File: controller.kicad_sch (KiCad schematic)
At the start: 57 parts, among them J1 Conn_ST_STDC14, J2 USB_C_Receptacle_USB2.0_14P, SW1 SW_Push, SW10 SW_Push, SW11 SW_Push, SW12 SW_Push, SW13 SW_Push, SW2 SW_Push, SW3 SW_Push, SW4 SW_Push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

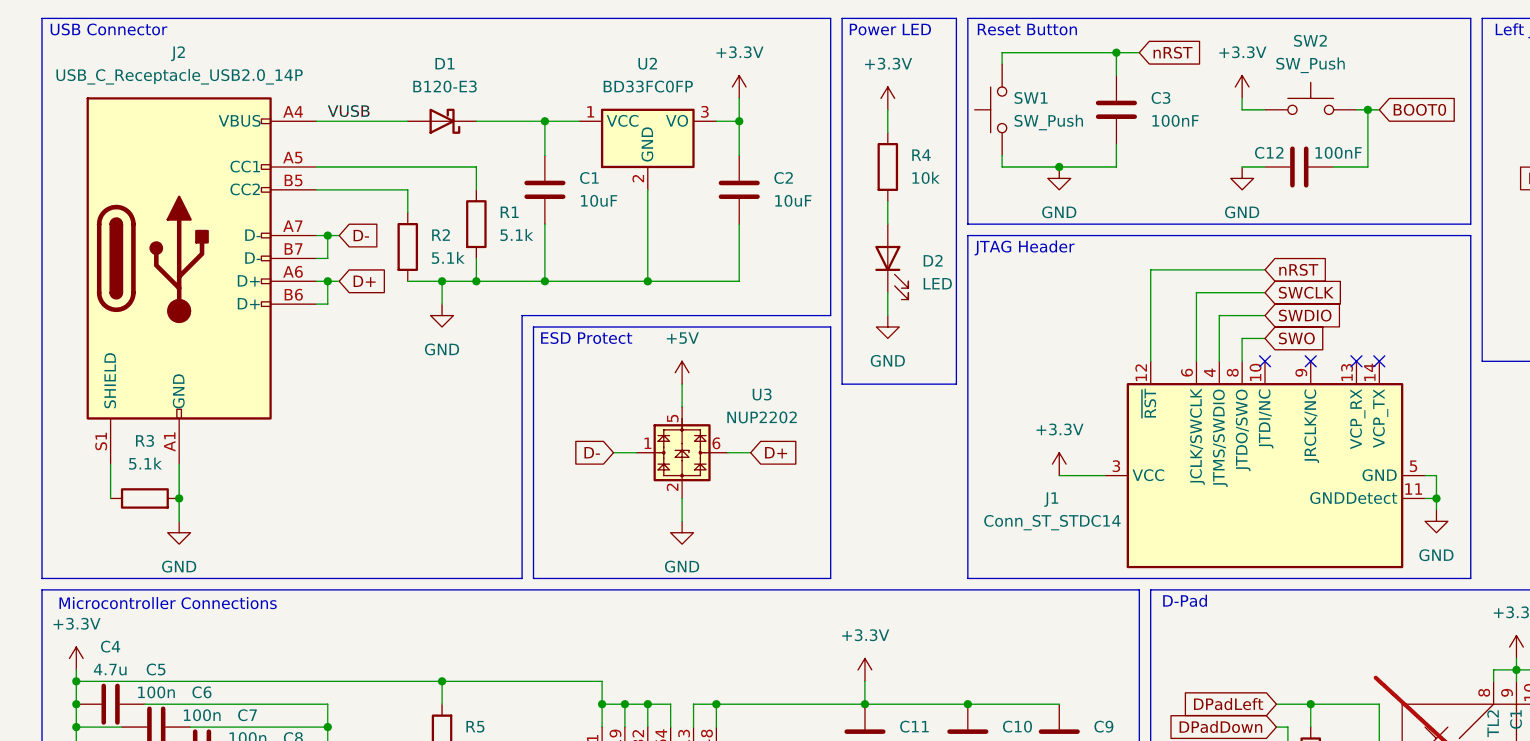
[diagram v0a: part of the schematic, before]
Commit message: add bom numbers
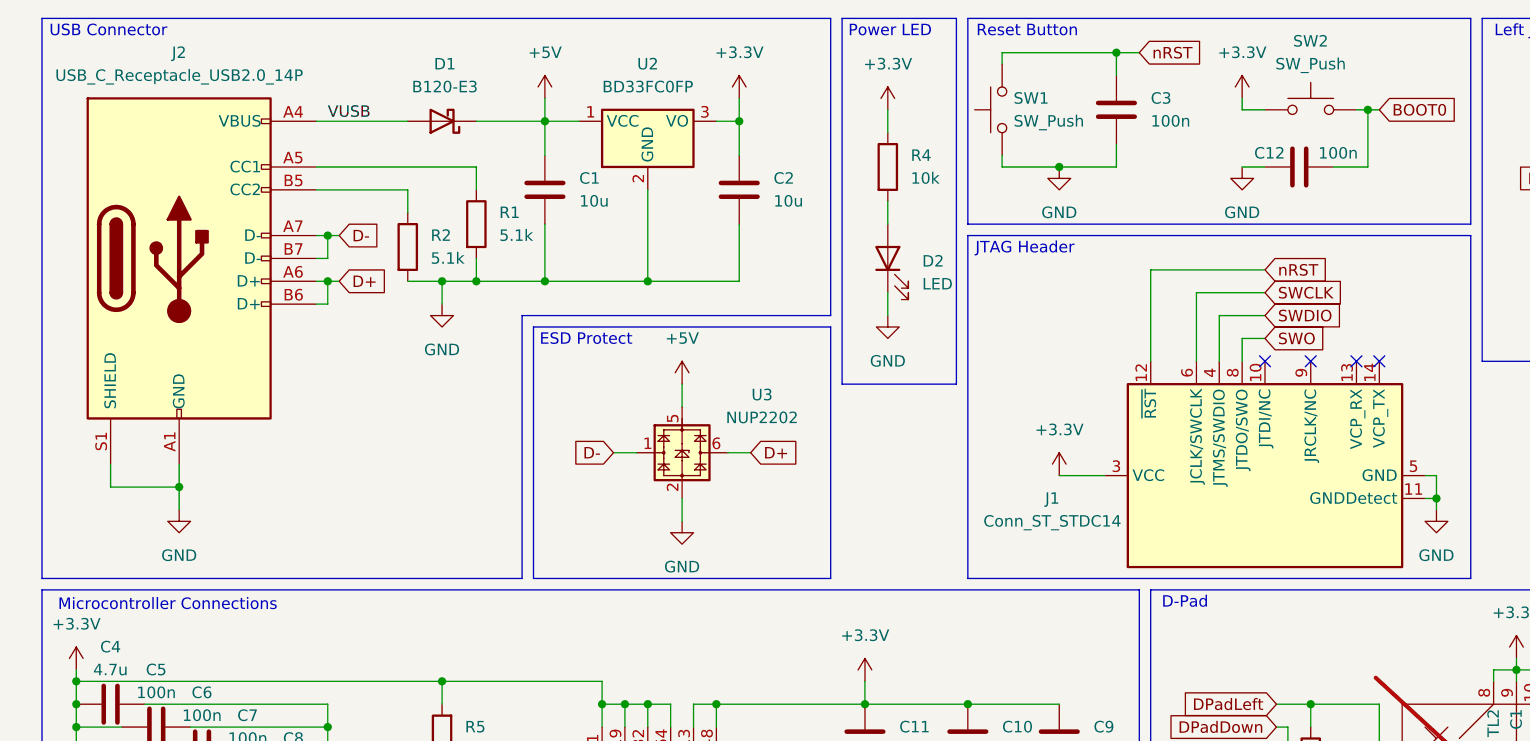
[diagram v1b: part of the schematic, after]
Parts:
- removed R3: 5.1k, Resistor_SMD:R_0201_0603Metric, symbol Device:R
- C1, C2: value 10uF -> 10u; footprint Capacitor_SMD:C_0201_0603Metric -> Capacitor_SMD:C_0402_1005Metric; MFR (none) -> Murata; MPN (none) -> GRM155R61A106ME11D; SPN (none) -> 490-GRM155R61A106ME11DCT-ND; SPR (none) -> DigiKey
- C10: MFR (none) -> Samsung; MPN (none) -> CL03A105MQ3CSNC; SPN (none) -> 1276-1325-1-ND; SPR (none) -> DigiKey
- C11, C5, C6, C7, C8: MFR (none) -> Murata; MPN (none) -> GRM033C71C104KE14D; SPN (none) -> 490-10387-1-ND; SPR (none) -> DigiKey
- C12, C3: value 100nF -> 100n; MFR (none) -> Murata; MPN (none) -> GRM033C71C104KE14D; SPN (none) -> 490-10387-1-ND; SPR (none) -> DigiKey
- C4: MFR (none) -> Murata; MPN (none) -> GRM035R60J475ME15D; SPN (none) -> 490-13230-1-ND; SPR (none) -> DigiKey
- C9: MFR (none) -> Murata; MPN (none) -> GRM033R71A103KA01D; SPN (none) -> 490-3194-1-ND; SPR (none) -> DigiKey
- D1: MFR (none) -> Vishay; MPN (none) -> B120-E3/61T; SPN (none) -> B120-E3/61TGICT-ND; SPR (none) -> DigiKey
- D2: MFR (none) -> Everlight; MPN (none) -> CSP0603AN101-WP30300563001-3T; SPN (none) -> 1080-CSP0603AN101-WP30300563001-3TCT-ND; SPR (none) -> DigiKey
- J1: MFR (none) -> Amphenol ICC; MPN (none) -> 20021111-00014T1LF; SPN (none) -> 609-4810-ND; SPR (none) -> DigiKey
- J2: MFR (none) -> GCT; MPN (none) -> USB4085-GF-A; SPN (none) -> 2073-USB4085-GF-ACT-ND; SPR (none) -> DigiKey
- R1, R2: MFR (none) -> YAGEO; MPN (none) -> RC0201FR-075K1L; SPN (none) -> YAG2741CT-ND; SPR (none) -> DigiKey
- R10, R11, R12, R13, R14, R15, R16, R17, R18, R19, R20, R21, R22, R23, R4, R5, R6, R7, R8, R9: MFR (none) -> Vishay Dale; MPN (none) -> CRCW020110K0FNED; SPN (none) -> 541-10.0KABCT-ND; SPR (none) -> DigiKey
- SW1, SW2: MFR (none) -> C&K; MPN (none) -> Y78B21110FP; SPN (none) -> 401-1426-1-ND; SPR (none) -> DigiKey
- SW10, SW11, SW8, SW9: footprint Button_Switch_SMD:SW_Push_1P1T-MP_NO_Horizontal_Alps_SKRTLAE010 -> EVQ-P7A01P:SW_EVQ-P7A01P_Single; MFR (none) -> Panasonic; MPN (none) -> EVQ-P7A01P; SPN (none) -> P16763CT-ND; SPR (none) -> DigiKey
- SW12, SW13: MFR (none) -> SCHURTER Inc.; MPN (none) -> 1301.9302; SPN (none) -> 486-3458-ND; SPR (none) -> DigiKey
- SW3, SW4, SW5, SW6: MFR (none) -> C&K; MPN (none) -> 10913247; SPN (none) -> 108-10913247CT-ND; SPR (none) -> DigiKey
- U1: MFR (none) -> STMicroelectronics; MPN (none) -> STM32L476RGT6; SPN (none) -> 497-15877-ND; SPR (none) -> DigiKey
- U2: MFR (none) -> Rohm Semiconductor; MPN (none) -> BD33FC0FP-E2; SPN (none) -> BD33FC0FP-E2CT-ND; SPR (none) -> DigiKey
- U3: MFR (none) -> onsemi; MPN (none) -> NUP2202W1T2G; SPN (none) -> NUP2202W1T2GOSCT-ND; SPR (none) -> DigiKey
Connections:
- net +5V: now also C1.1, D1.1 (K), U2.1 (VCC)
- net GND: now also J2.S1 (SHIELD)

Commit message: some minor trace changes
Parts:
- renumbered R18 to R17, R17 to R18
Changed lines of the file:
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@@
 		(dnp no)
 		(fields_autoplaced yes)
-		(property "Reference" "R17"
+		(property "Reference" "R18"
 			(at 156.21 93.9799 0)
 			(effects
@@
 			(project "controller"
 				(path "/8767df91-471e-42dd-a6da-5f13f49512a3"
-					(reference "R17")
+					(reference "R18")
 					(unit 1)
 				)
@@
 		(dnp no)
 		(fields_autoplaced yes)
-		(property "Reference" "R18"
+		(property "Reference" "R17"
 			(at 158.75 105.4099 0)
 			(effects
@@
 			(project "controller"
 				(path "/8767df91-471e-42dd-a6da-5f13f49512a3"
-					(reference "R18")
-					(unit 1)
-				)
+					(reference "R17")
+					(unit 1)
+				)

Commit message: add 3220 component
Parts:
- J1: footprint Connector_PinHeader_1.27mm:PinHeader_2x07_P1.27mm_Vertical -> 3220_14_0100:CONN14_3220-14_CNC
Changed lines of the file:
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@@
 			)
 		)
-		(property "Footprint" "Connector_PinHeader_1.27mm:PinHeader_2x07_P1.27mm_Vertical"
+		(property "Footprint" "3220_14_0100:CONN14_3220-14_CNC"
 			(at 148.59 63.5 0)
 			(effects

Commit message: change symbol properties to new version
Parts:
- J1: MFR Amphenol ICC -> CNC Tech; MPN 20021111-00014T1LF -> 3220-14-0100-00; SPN 609-4810-ND -> 1175-1630-ND
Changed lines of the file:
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@@
 			)
 		)
-		(property "MFR" "Amphenol ICC"
+		(property "MFR" "CNC Tech"
 			(at 148.59 63.5 90)
 			(effects
@@
 			)
 		)
-		(property "MPN" "20021111-00014T1LF"
+		(property "MPN" "3220-14-0100-00"
 			(at 148.59 63.5 90)
 			(effects
@@
 			)
 		)
-		(property "SPN" "609-4810-ND"
+		(property "SPN" "1175-1630-ND"
 			(at 148.59 63.5 90)
 			(effects
